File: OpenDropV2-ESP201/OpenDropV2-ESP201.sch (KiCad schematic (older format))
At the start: 194 parts, among them J1 DC_JACK, P6 CONN_01X30, Q1 BSS138, Q2 BSS138, Q3 BSS138, Q4 BSS138, Q5 BSS138, SW1 SW_PUSH, SW2 SW_PUSH, SW5 SPST, T1 IRF 840S, U1 MAX1771ESA, U2 HV507, U3 ESP-201, U4 HV507

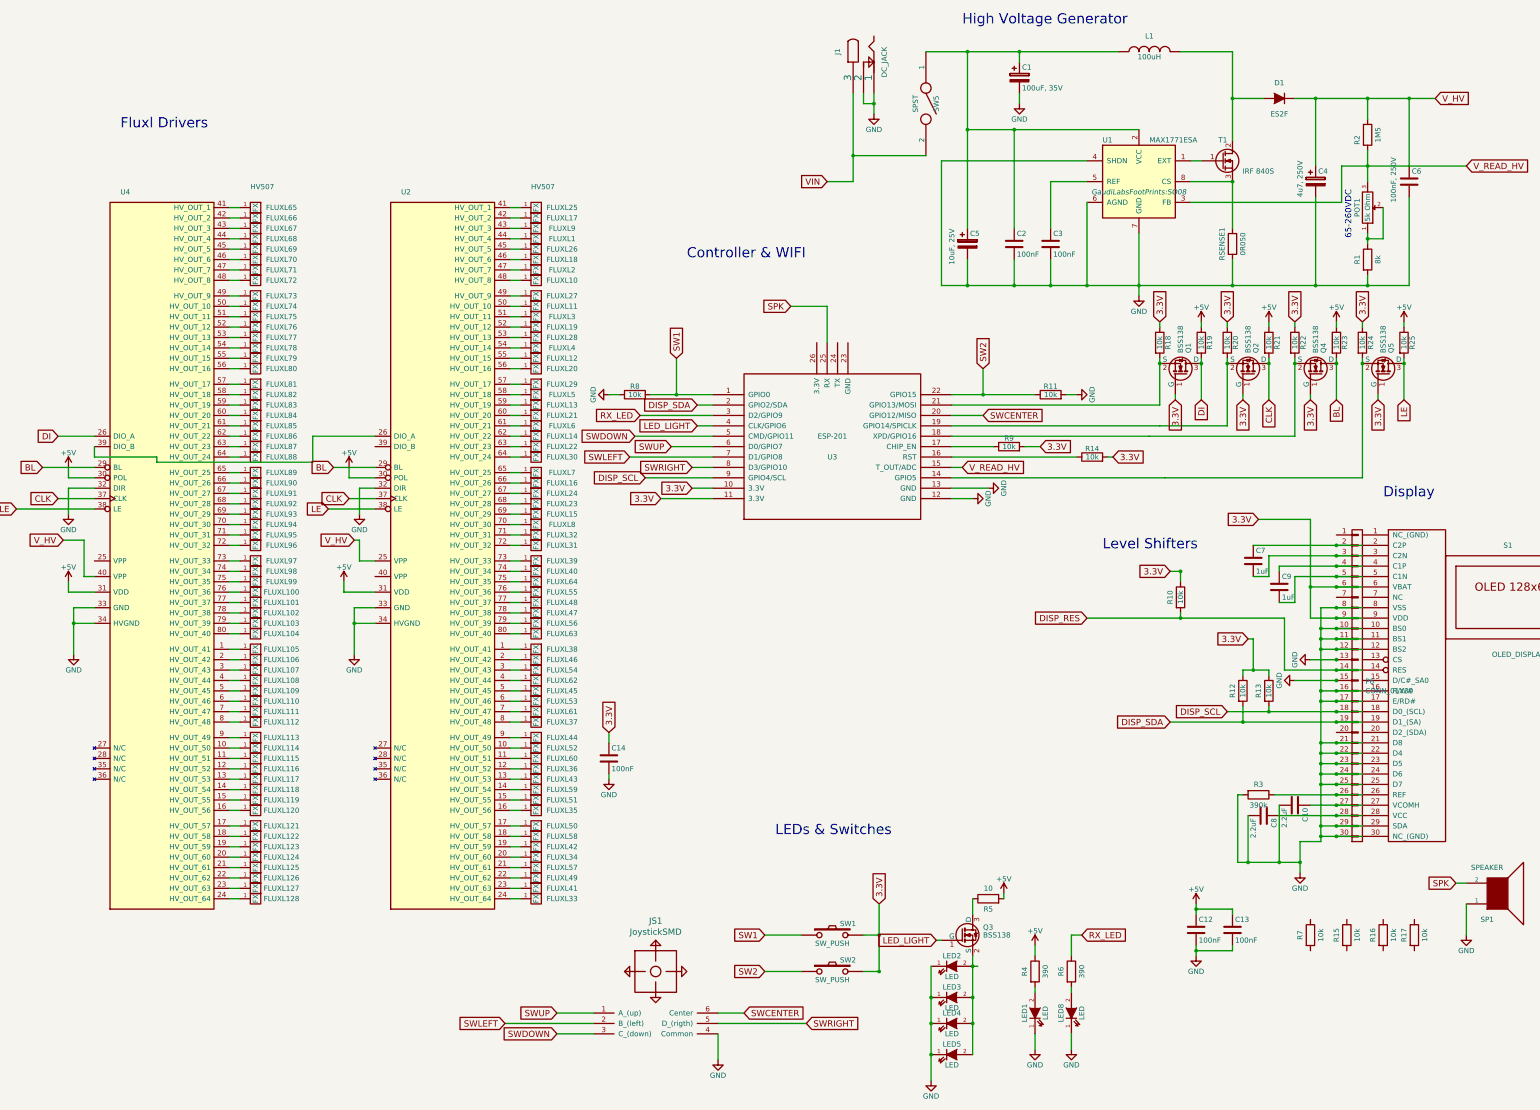
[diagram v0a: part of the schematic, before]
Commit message: put fet at ground for led lights
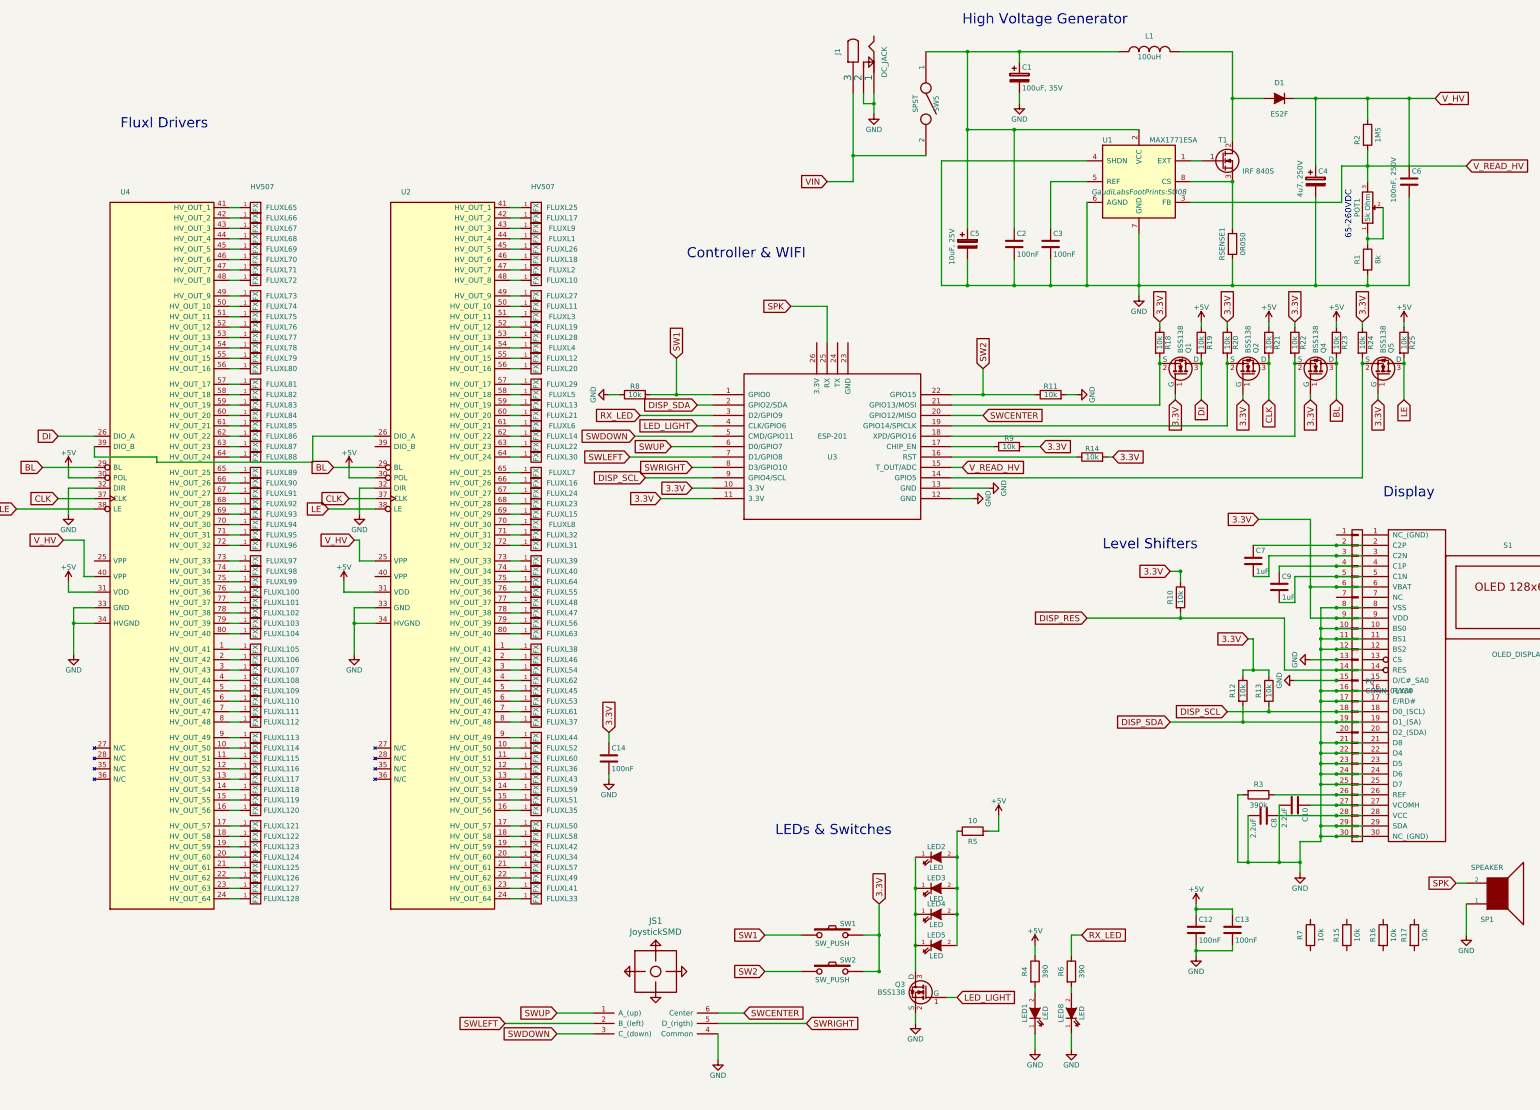
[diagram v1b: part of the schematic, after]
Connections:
- net GND: now also Q3.2 (S); no longer LED2.1 (K), LED3.1 (K), LED4.1 (K), LED5.1 (K)
- net at LED2.2 (A), LED3.2 (A), LED4.2 (A)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: now also R5.1; no longer Q3.2 (S)
- net at Q3.3 (D): now also LED2.1 (K), LED3.1 (K), LED4.1 (K), LED5.1 (K); no longer R5.1
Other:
- moved on the sheet: LED2, LED3, LED4, LED5, Q3, R5
